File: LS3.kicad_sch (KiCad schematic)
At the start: 6 parts, among them Q5 NCE4080K, Q6 NCE4080K, Q7 NCE4080K

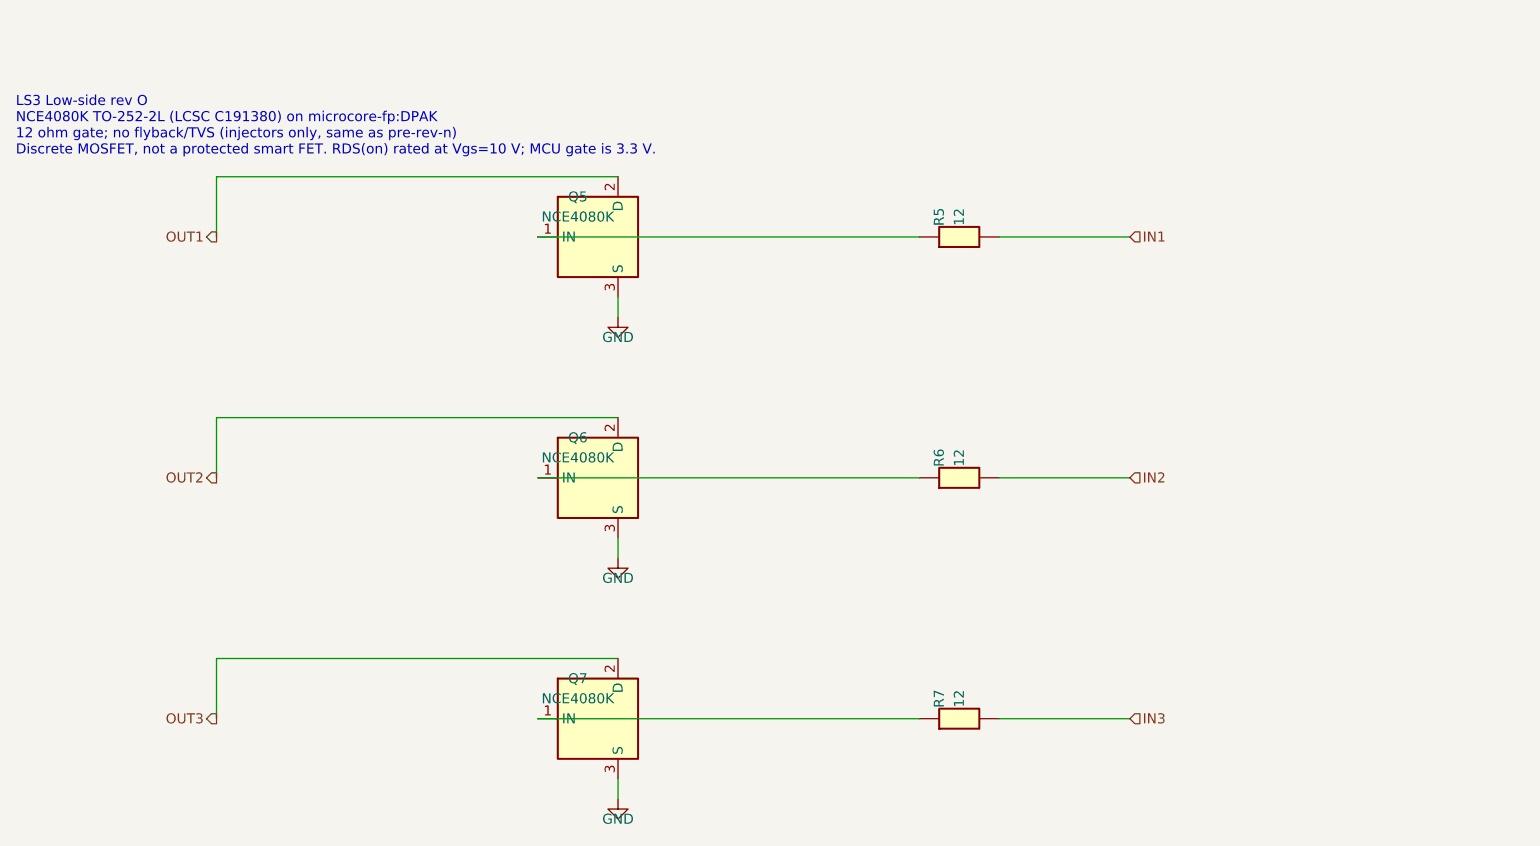
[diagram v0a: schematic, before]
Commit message: Rev p: AOD4184A (C99124) + LS US1M/SMAJ33A + DRC (#9)
* Rev p: AOD4184A on Q1-Q7, LS flyback+TVS, frame short fixes

Quintin chose AOD4184A (LCSC C99124) plus TVS for budget and reliability.
Q5-Q7 get the existing US1M flyback and SMAJ33A. Injector/VR frame shorts
on the board copper are cleared; Hellen module pad-G noise stays documented.

Co-authored-by: Quintin <quintinbannink42@users.noreply.github.com>

* Rev p: keep Q1-Q7 as NCE4080K; LS US1M+SMAJ33A stays

Budget and reliability first. No FET or BOM upgrade and no DPAK land change. Low-side clamps stay the injector US1M and SMAJ33A already in the BOM.

Co-authored-by: Quintin <quintinbannink42@users.noreply.github.com>

---------

Co-authored-by: Quintin <quintinbannink42@users.noreply.github.com>
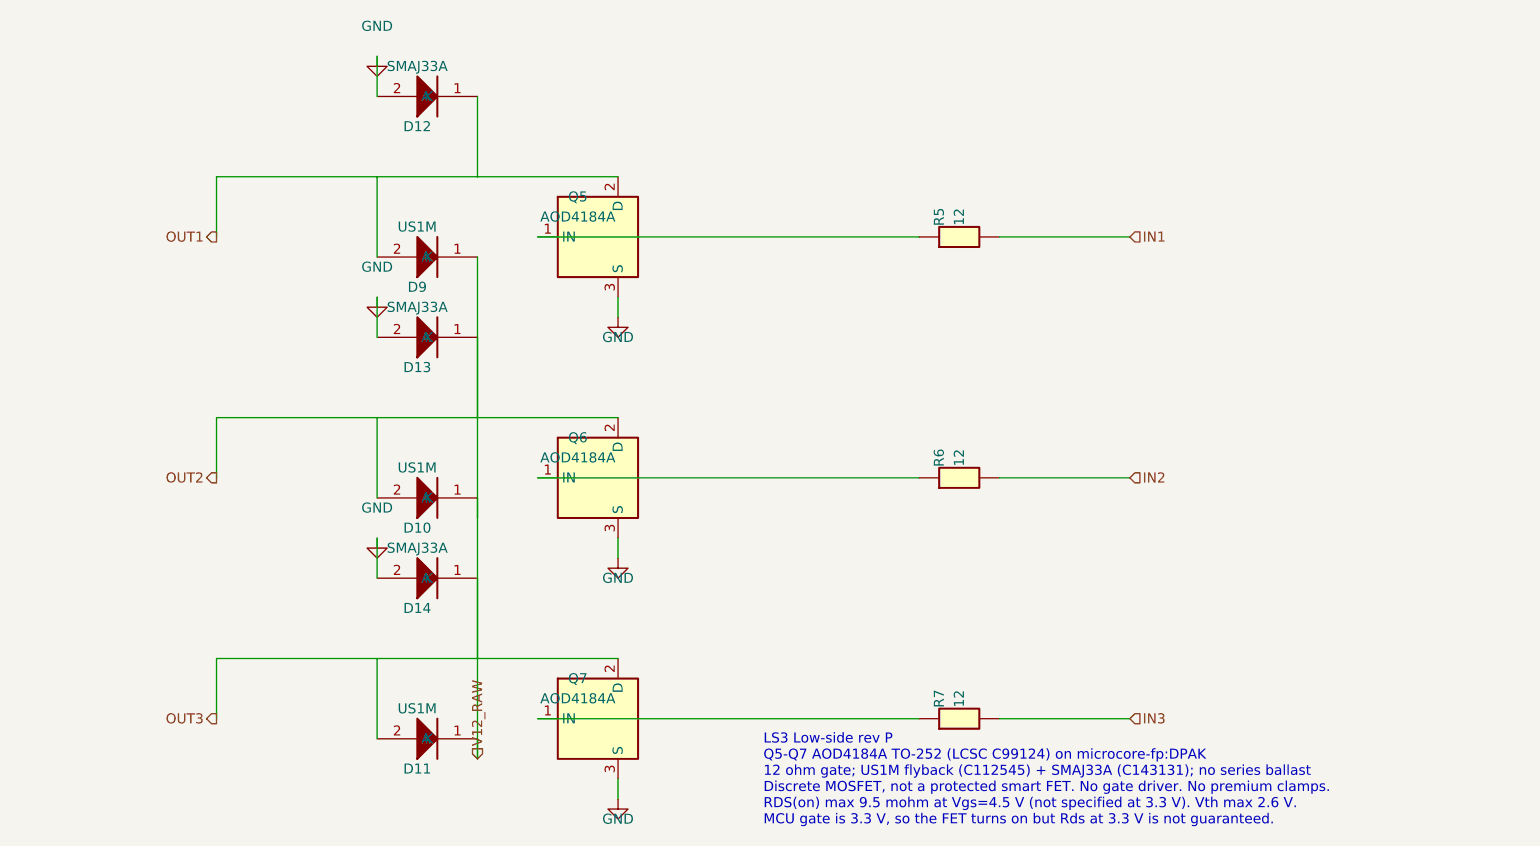
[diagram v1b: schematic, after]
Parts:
- added D10, D11, D9: US1M, microcore-fp:DO214AC, symbol hellen-one-common:1N4148WS
- added D12, D13, D14: SMAJ33A, microcore-fp:DO214AC, symbol hellen-one-common:1N4148WS
- Q5, Q6, Q7: value NCE4080K -> AOD4184A
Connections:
- net OUT3 is gone; now on net OUT2: Q7.2 (D)
- net GND: now also D12.2 (A), D13.2 (A), D14.2 (A)
- net OUT1: now also D12.1 (K), D9.2 (A)
- net OUT2: now also D10.1 (K), D10.2 (A), D11.1 (K), D11.2 (A), D13.1 (K), D14.1 (K), D9.1 (K)
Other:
- note added: "LS3 Low-side rev P Q5-Q7 AOD4184A TO-252 (LCSC C99124) on microcore-fp:DPAK 12 ohm gate; US1M flyback (C112545) + SMAJ33A (C143131); no series ballast Discrete MOSFET, not a protected smart FET. No gate driver. No premium clamps. RDS(on) max 9.5 mohm at Vgs=4.5 V (not specified at 3.3 V). Vth max 2.6 V. MCU gate is 3.3 V, so the FET turns on but Rds at 3.3 V is not guaranteed."
- note removed: "LS3 Low-side rev O NCE4080K TO-252-2L (LCSC C191380) on microcore-fp:DPAK 12 ohm gate; no flyback/TVS (injectors only, same as pre-rev-n) Discrete MOSFET, not a protected smart FET. RDS(on) rated at Vgs=10 V; MCU gate is 3.3 V."
